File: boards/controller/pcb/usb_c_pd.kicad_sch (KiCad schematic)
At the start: 12 parts, among them J201 699C124-2A6-111, U201 USBLC6-2SC6, U202 TCPP01-M12, U203 ISZ065N03L5SATMA1

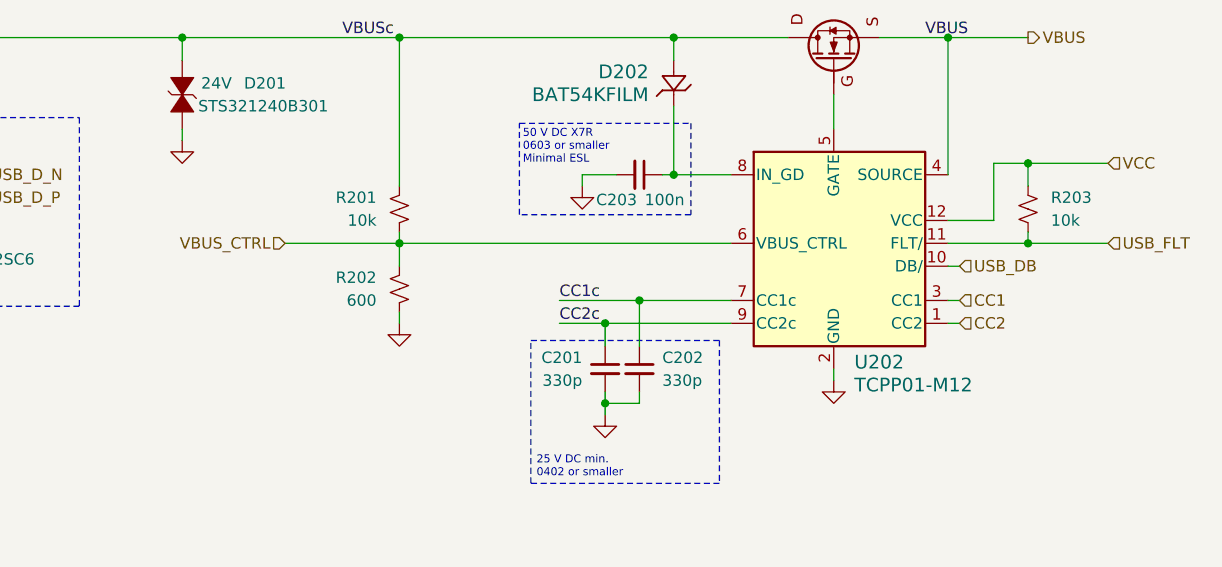
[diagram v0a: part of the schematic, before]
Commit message: controller: pcb: Update schematic
Signed-off-by: Nicholas Loehrke <nicholasnloehrke@gmail.com>
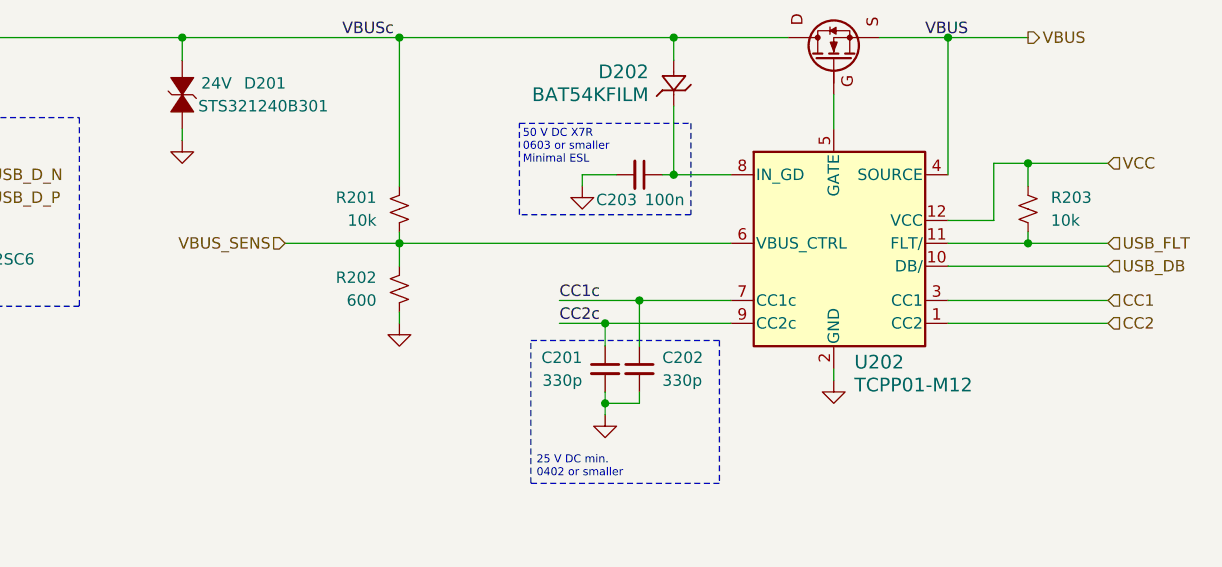
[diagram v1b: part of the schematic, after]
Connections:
- net VBUS_CTRL renamed VBUS_SENS
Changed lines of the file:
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@@
 	(wire
 		(pts
-			(xy 214.63 105.41) (xy 215.9 105.41)
+			(xy 214.63 105.41) (xy 232.41 105.41)
 		)
 		(stroke
@@
 	(wire
 		(pts
-			(xy 214.63 99.06) (xy 215.9 99.06)
+			(xy 214.63 99.06) (xy 232.41 99.06)
 		)
 		(stroke
@@
 	(wire
 		(pts
-			(xy 214.63 102.87) (xy 215.9 102.87)
+			(xy 214.63 102.87) (xy 232.41 102.87)
 		)
 		(stroke
@@
 	(hierarchical_label "USB_DB"
 		(shape input)
-		(at 215.9 99.06 0)
+		(at 232.41 99.06 0)
 		(effects
 			(font
@@
 		)
 	)
-	(hierarchical_label "VBUS_CTRL"
+	(hierarchical_label "VBUS_SENS"
 		(shape input)
 		(at 140.97 96.52 180)
@@
 	(hierarchical_label "CC2"
 		(shape input)
-		(at 215.9 105.41 0)
+		(at 232.41 105.41 0)
 		(effects
 			(font
@@
 	(hierarchical_label "CC1"
 		(shape input)
-		(at 215.9 102.87 0)
-		(effects
-			(font
+		(at 232.41 102.87 0)
+		(effects
+			(font

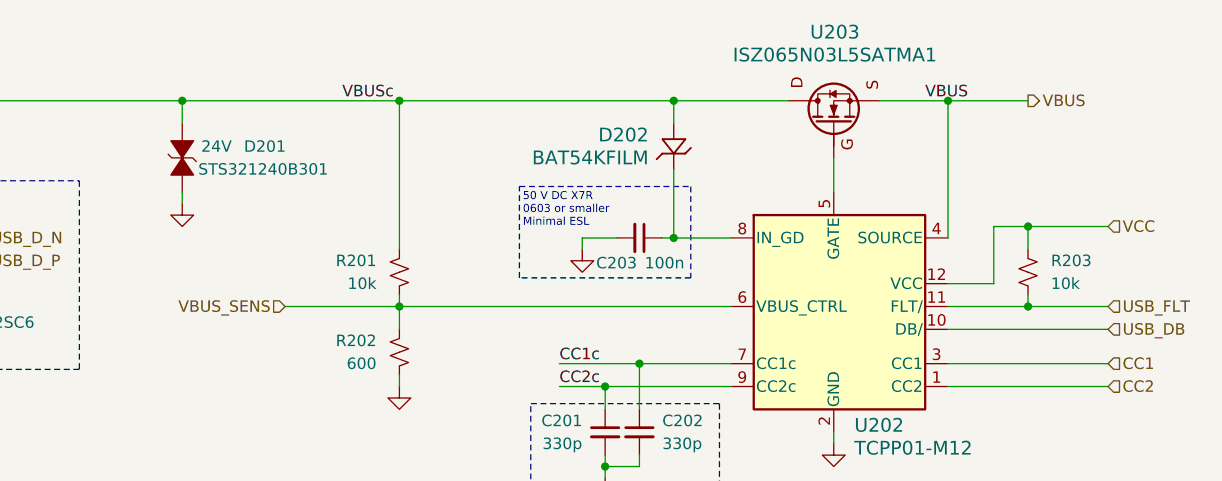
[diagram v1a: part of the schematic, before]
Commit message: controller: pcb: Update schematic
Signed-off-by: Nicholas Loehrke <nicholasnloehrke@gmail.com>
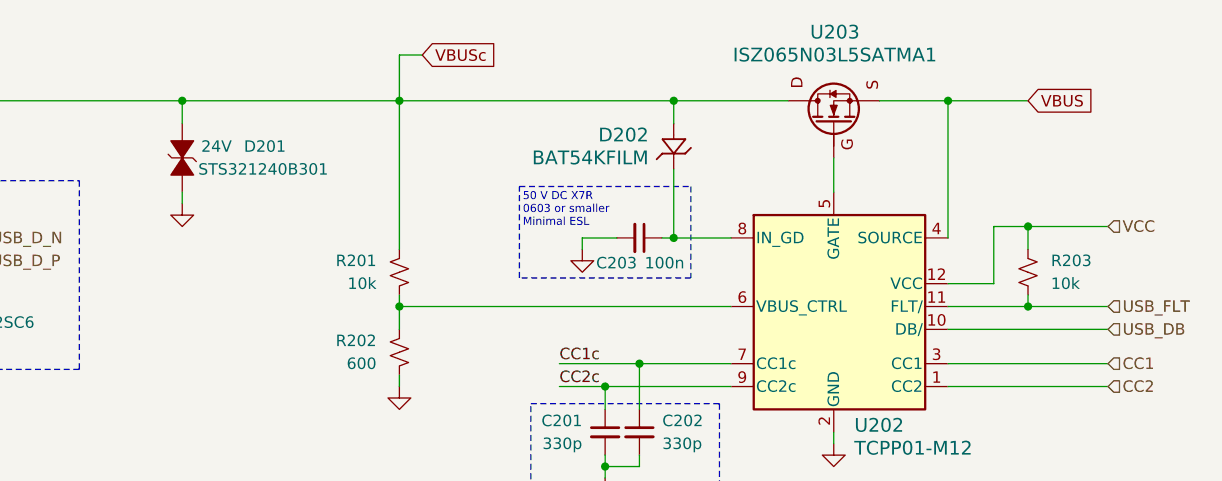
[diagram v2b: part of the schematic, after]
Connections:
- net VBUS_SENS: no longer names the net of R201.2, R202.1, U202.6 (VBUS_CTRL)
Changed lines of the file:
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@@
+	(wire
+		(pts
+			(xy 153.67 68.58) (xy 156.21 68.58)
+		)
+		(stroke
+			(width 0)
+			(type default)
+		)
+	)
 	(wire
 		(pts
@@
 	(wire
 		(pts
-			(xy 140.97 96.52) (xy 153.67 96.52)
-		)
-		(stroke
-			(width 0)
-			(type default)
-		)
-	)
-	(wire
-		(pts
 			(xy 171.45 105.41) (xy 176.53 105.41)
 		)
@@
 	(wire
 		(pts
+			(xy 153.67 68.58) (xy 153.67 73.66)
+		)
+		(stroke
+			(width 0)
+			(type default)
+		)
+	)
+	(wire
+		(pts
 			(xy 184.15 73.66) (xy 196.85 73.66)
 		)
@@
 			(width 0.508)
 			(type default)
-		)
-	)
-	(label "VBUSc"
-		(at 147.32 73.66 0)
-		(effects
-			(font
-				(size 1.27 1.27)
-			)
-			(justify left bottom)
 		)
 	)
@@
 		)
 	)
-	(label "VBUS"
-		(at 212.09 73.66 0)
-		(effects
-			(font
-				(size 1.27 1.27)
-			)
-			(justify left bottom)
+	(global_label "VBUSc"
+		(shape input)
+		(at 156.21 68.58 0)
+		(fields_autoplaced yes)
+		(effects
+			(font
+				(size 1.27 1.27)
+			)
+			(justify left)
+		)
+		(property "Intersheetrefs" "${INTERSHEET_REFS}"
+			(at 165.1824 68.58 0)
+			(effects
+				(font
+					(size 1.27 1.27)
+				)
+				(justify left)
+				(hide yes)
+			)
+		)
+	)
+	(global_label "VBUS"
+		(shape input)
+		(at 223.52 73.66 0)
+		(fields_autoplaced yes)
+		(effects
+			(font
+				(size 1.27 1.27)
+			)
+			(justify left)
+		)
+		(property "Intersheetrefs" "${INTERSHEET_REFS}"
+			(at 231.4038 73.66 0)
+			(effects
+				(font
+					(size 1.27 1.27)
+				)
+				(justify left)
+				(hide yes)
+			)
 		)
 	)
@@
 		(effects
 			(font
-				(size 1.27 1.27)
-			)
-			(justify left)
-		)
-	)
-	(hierarchical_label "VBUS_SENS"
-		(shape input)
-		(at 140.97 96.52 180)
-		(effects
-			(font
-				(size 1.27 1.27)
-			)
-			(justify right)
-		)
-	)
-	(hierarchical_label "VBUS"
-		(shape output)
-		(at 223.52 73.66 0)
-		(effects
-			(font

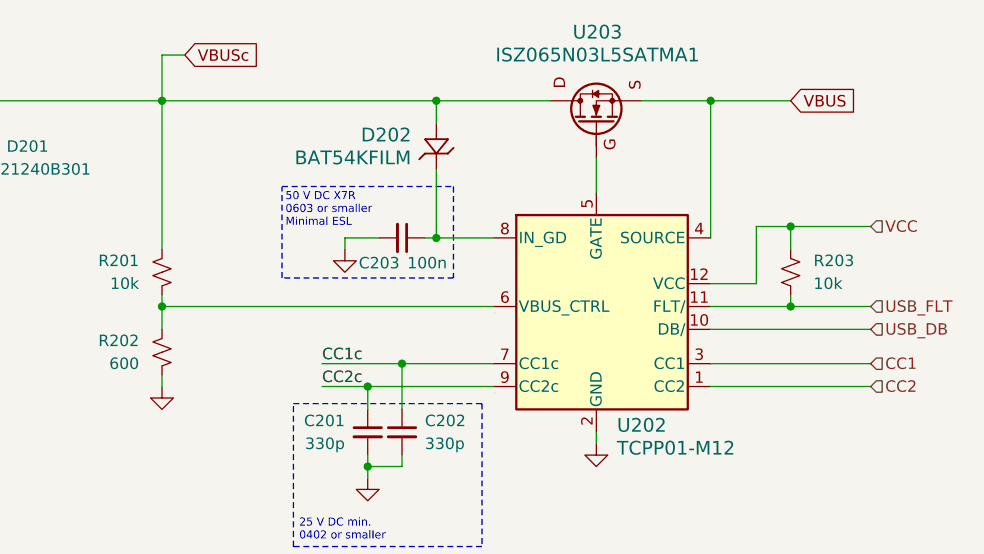
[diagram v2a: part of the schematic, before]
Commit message: controller: pcb: Update schematic
Signed-off-by: Nicholas Loehrke <nicholasnloehrke@gmail.com>
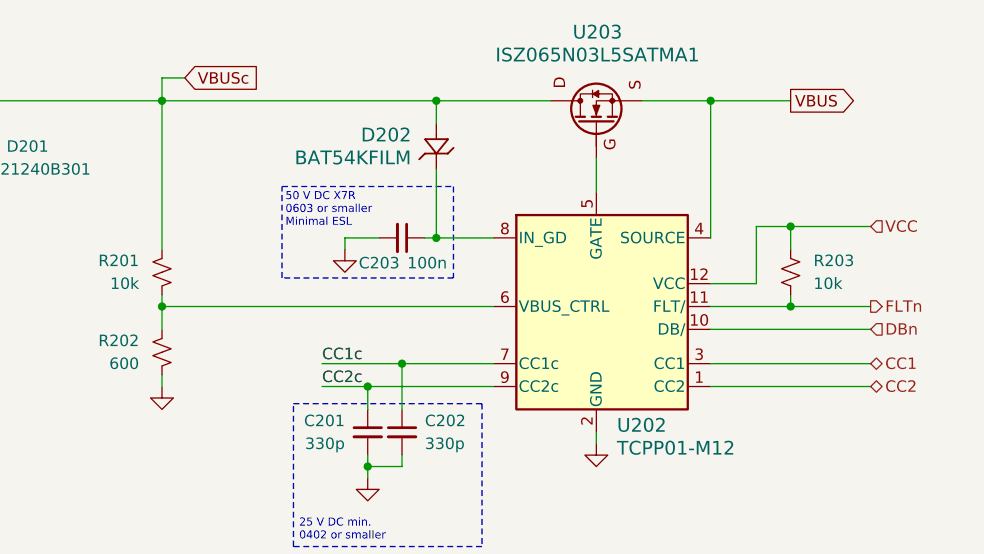
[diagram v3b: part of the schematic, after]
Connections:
- net USB_DB renamed DBn
- net USB_FLT renamed FLTn
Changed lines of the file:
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@@
 	(wire
 		(pts
-			(xy 153.67 68.58) (xy 156.21 68.58)
+			(xy 153.67 71.12) (xy 156.21 71.12)
 		)
 		(stroke
@@
 	(wire
 		(pts
-			(xy 153.67 68.58) (xy 153.67 73.66)
+			(xy 153.67 71.12) (xy 153.67 73.66)
 		)
 		(stroke
@@
 	(global_label "VBUSc"
 		(shape input)
-		(at 156.21 68.58 0)
+		(at 156.21 71.12 0)
 		(fields_autoplaced yes)
 		(effects
@@
 		)
 		(property "Intersheetrefs" "${INTERSHEET_REFS}"
-			(at 165.1824 68.58 0)
+			(at 165.1824 71.12 0)
 			(effects
 				(font
@@
 	)
 	(global_label "VBUS"
-		(shape input)
+		(shape output)
 		(at 223.52 73.66 0)
 		(fields_autoplaced yes)
@@
 		)
 	)
-	(hierarchical_label "USB_DB"
+	(hierarchical_label "DBn"
 		(shape input)
 		(at 232.41 99.06 0)
@@
 		)
 	)
-	(hierarchical_label "USB_FLT"
-		(shape input)
+	(hierarchical_label "FLTn"
+		(shape output)
 		(at 232.41 96.52 0)
 		(effects
@@
 	)
 	(hierarchical_label "CC2"
-		(shape input)
+		(shape bidirectional)
 		(at 232.41 105.41 0)
 		(effects
@@
 	)
 	(hierarchical_label "CC1"
-		(shape input)
+		(shape bidirectional)
 		(at 232.41 102.87 0)
 		(effects

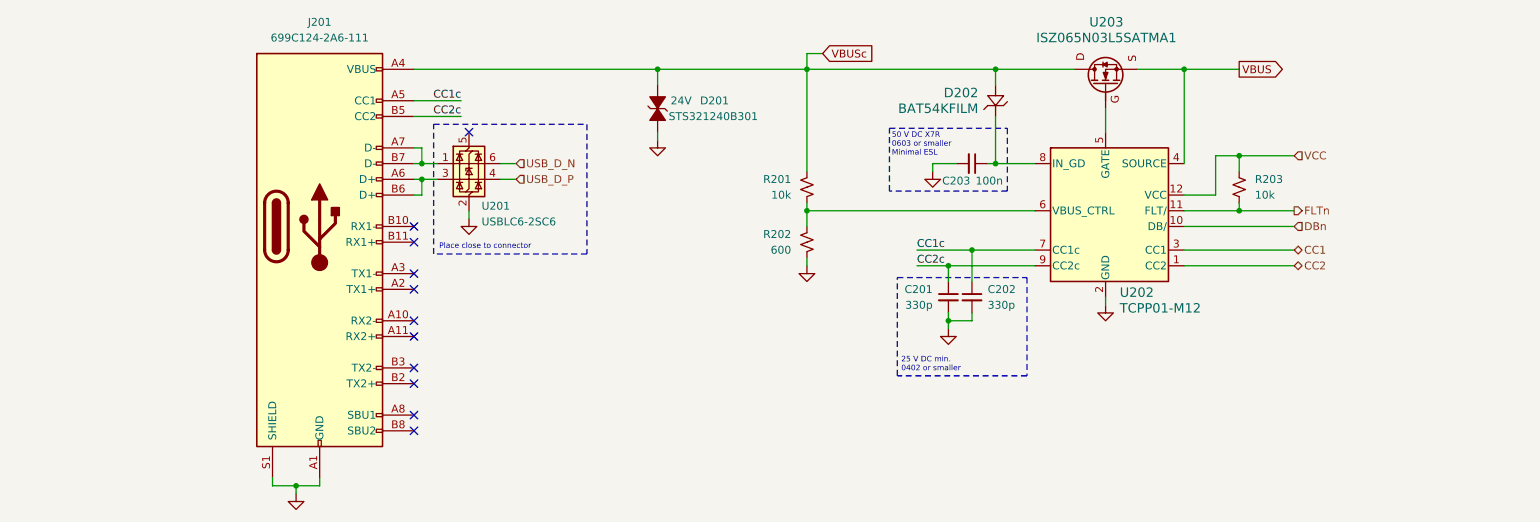
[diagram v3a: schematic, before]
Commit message: controller: pcb: Update schematic
Signed-off-by: Nicholas Loehrke <nicholasnloehrke@gmail.com>
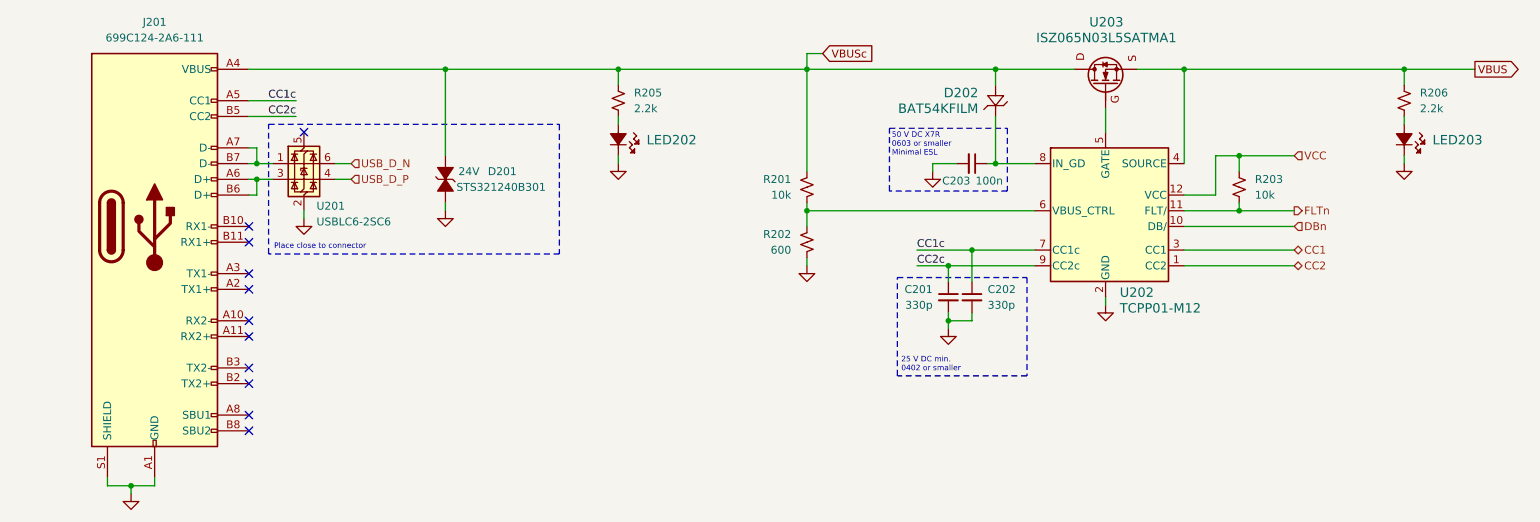
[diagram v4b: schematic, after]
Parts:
- added LED202, LED203: B1911PG--20D000514U1930, LED_B1911PG--20D000514U1930_HVK, symbol B1911PG--20D000514U1930:B1911PG--20D000514U1930
- added R205, R206: 2.2k, symbol Device:R_Small_US
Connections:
- net GND: now also LED202.1, LED203.1
- net VBUS: now also R206.1
- net VBUSc: now also R205.1
- new net: LED202.2, R205.2
- new net: LED203.2, R206.2
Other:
- moved on the sheet: D201, J201, U201

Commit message: controller: pcb: Update schematic
Signed-off-by: Nicholas Loehrke <nicholasnloehrke@gmail.com>
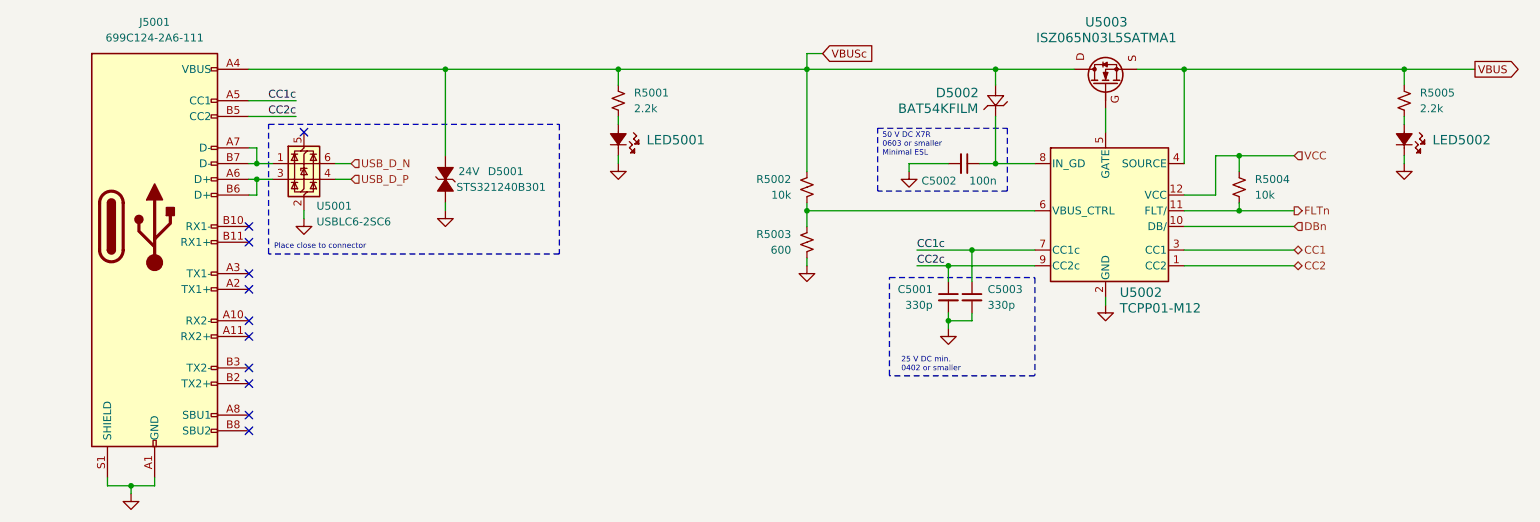
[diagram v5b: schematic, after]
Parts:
- renumbered C201 to C5001, C203 to C5002, C202 to C5003, D201 to D5001, D202 to D5002, J201 to J5001, LED202 to LED5001, LED203 to LED5002, R205 to R5001, R201 to R5002, R202 to R5003, R203 to R5004, R206 to R5005, U201 to U5001, U202 to U5002, U203 to U5003
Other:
- moved on the sheet: C5002

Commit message: controller: pcb: Update schematic
- Add power button pmos gate voltage clamp
- Add TVS diodes on encoders

Signed-off-by: Nicholas Loehrke <nicholasnloehrke@gmail.com>
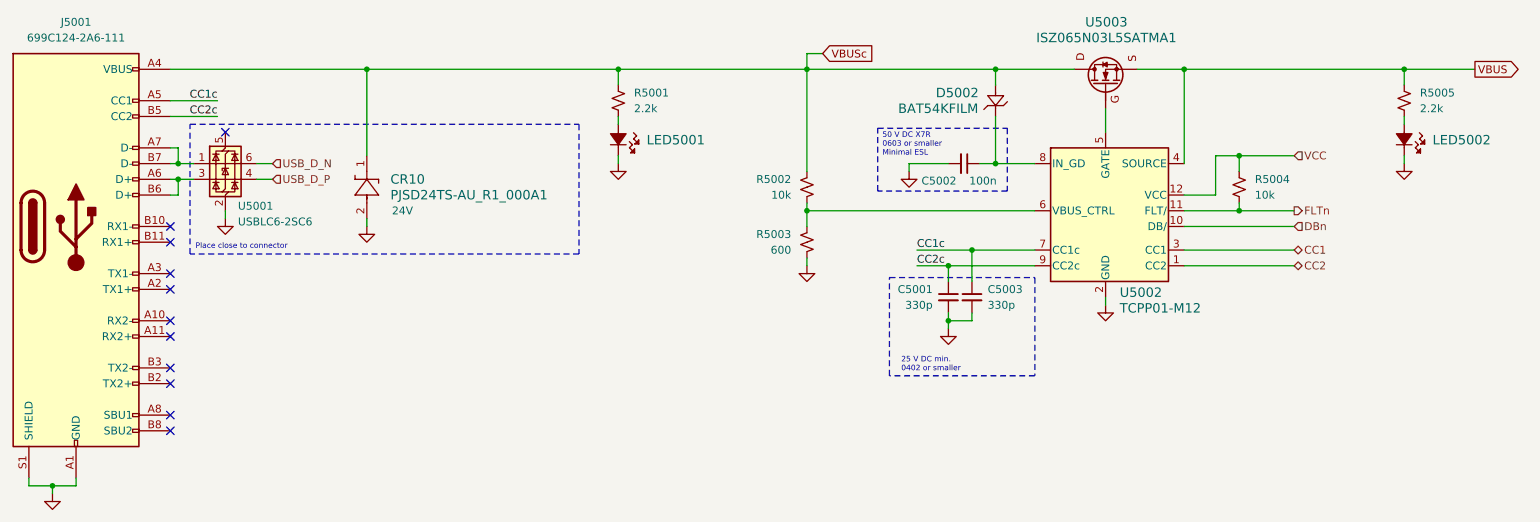
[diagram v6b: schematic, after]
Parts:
- removed D5001: 24V, STS321240B301:STS321240B301, symbol STS321240B301:STS321240B301
- added CR10: PJSD24TS-AU_R1_000A1, CR_SOD-523_PNJ, symbol PJSD24TS-AU_R1_000A1:PJSD24TS-AU_R1_000A1
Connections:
- net GND: now also CR10.2
- net VBUSc: now also CR10.1
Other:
- moved on the sheet: J5001, U5001

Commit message: controller: pcb: Update schematic
Signed-off-by: Nicholas Loehrke <nicholasnloehrke@gmail.com>
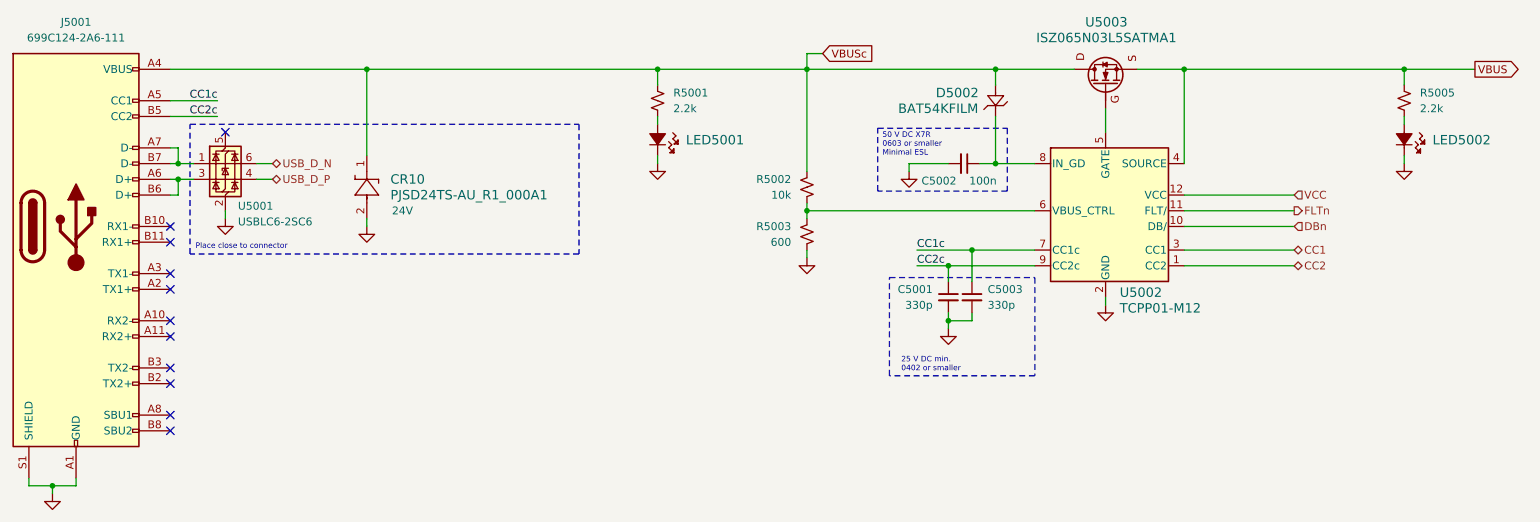
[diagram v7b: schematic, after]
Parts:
- removed R5004: 10k, symbol Device:R_Small_US
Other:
- moved on the sheet: LED5001, R5001, R5003
